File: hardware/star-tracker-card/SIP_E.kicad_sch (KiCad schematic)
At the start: 1 part, among them U7 OSD3358-512M-BSM

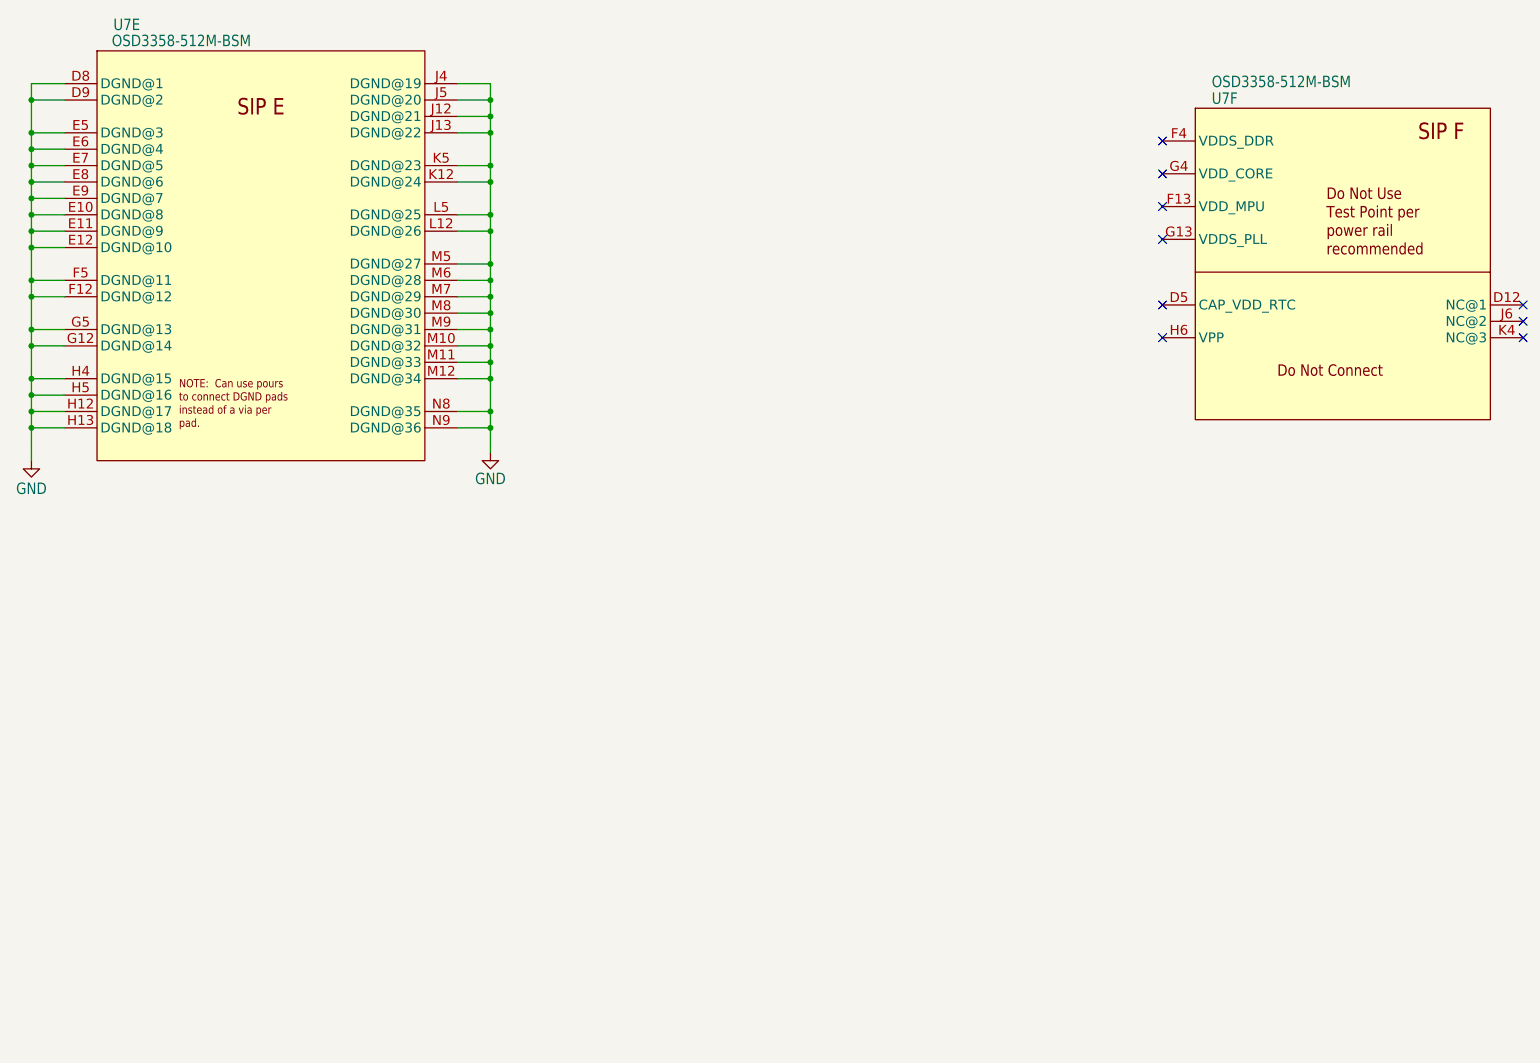
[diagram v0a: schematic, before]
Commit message: Big almost-done cleanup
Fixed a bunch of things in the schematic. Compared against C3 Octavo. Fixed all weird ERCs. Cleaned up a lot of planes on the layout. Moved uart switch, rerouted a bunch of traces for better layout. Fixed library issues, and board/sch sync issues.
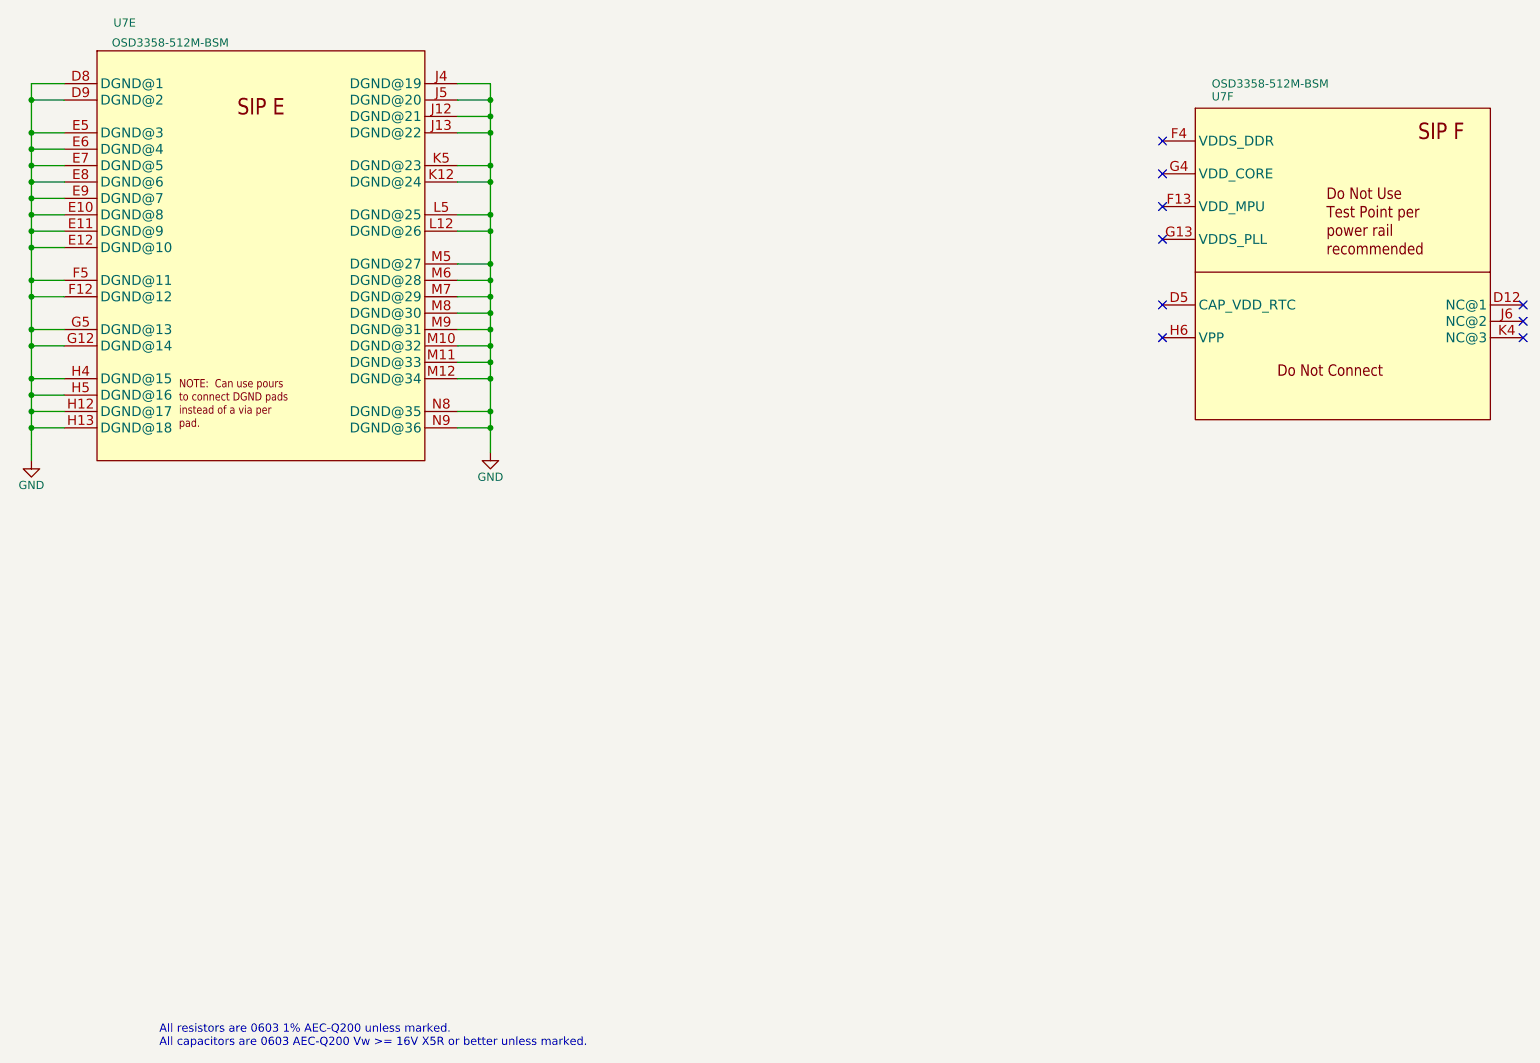
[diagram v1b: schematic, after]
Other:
- note added: "All resistors are 0603 1% AEC-Q200 unless marked. All capacitors are 0603 AEC-Q200 Vw >= 16V X5R or better unless marked."
- company: (none) -> Portland State Aerospace Society
- title: (none) -> OreSat Star Tracker
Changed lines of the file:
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@@
 	(generator_version "9.0")
 	(paper "B")
+	(title_block
+		(title "OreSat Star Tracker")
+		(date "2026-04-15")
+		(rev "1.3")
+		(company "Portland State Aerospace Society")
+	)
+	(text "All resistors are 0603 1% AEC-Q200 unless marked.\nAll capacitors are 0603 AEC-Q200 Vw >= 16V X5R or better unless marked."
+		(exclude_from_sim no)
+		(at 112.522 266.192 0)
+		(effects
+			(font
+				(size 1.27 1.27)
+			)
+			(justify left bottom)
+		)
+	)
 	(junction
 		(at 163.83 129.54)
@@
 			(effects
 				(font
-					(size 1.778 1.5113)
+					(size 1.27 1.27)
 				)
 				(justify left top)
@@
 			(effects
 				(font
-					(size 1.778 1.5113)
+					(size 1.27 1.27)
 				)
 				(justify left bottom)
@@
 		(on_board yes)
 		(dnp no)
-		(property "Reference" "#GND74"
-			(at 163.83 173.99 0)
+		(property "Reference" "#PWR74"
+			(at 163.83 180.34 0)
 			(effects
 				(font
@@
 		)
 		(property "Value" "GND"
-			(at 163.83 177.038 0)
+			(at 163.83 177.8 0)
 			(effects
 				(font
-					(size 1.778 1.5113)
-				)
-				(justify top)
+					(size 1.27 1.27)
+				)
 			)
 		)
@@
 			(project "star-tracker-card"
 				(path "/324e9eb5-7420-4b7e-862c-cc20bb28618a/eb575624-9a53-42ad-b889-70334a877908"
-					(reference "#GND74")
+					(reference "#PWR74")
 					(unit 1)
 				)
@@
 			(effects
 				(font
-					(size 1.778 1.5113)
+					(size 1.27 1.27)
 				)
 				(justify left top)
@@
 			(effects
 				(font
-					(size 1.778 1.5113)
+					(size 1.27 1.27)
 				)
 				(justify left bottom)
@@
 		(on_board yes)
 		(dnp no)
-		(property "Reference" "#GND73"
-			(at 92.71 175.26 0)
+		(property "Reference" "#PWR73"
+			(at 92.71 181.61 0)
 			(effects
 				(font
@@
 		)
 		(property "Value" "GND"
-			(at 92.71 178.562 0)
+			(at 92.71 179.07 0)
 			(effects
 				(font
-					(size 1.778 1.5113)
-				)
-				(justify top)
+					(size 1.27 1.27)
+				)
 			)
 		)
@@
 			(project "star-tracker-card"
 				(path "/324e9eb5-7420-4b7e-862c-cc20bb28618a/eb575624-9a53-42ad-b889-70334a877908"
-					(reference "#GND73")
+					(reference "#PWR73")
 					(unit 1)
 				)

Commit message: BOM 99% completed, push for final review
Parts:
- U7: DIS (none) -> DigiKey; DPN (none) -> 1676-OSD3358-1G-ISM-ND; MFR (none) -> Octavo Systems LLC; MPN (none) -> OSD3358-1G-ISM
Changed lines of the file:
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@@
 (kicad_sch
-	(version 20250114)
+	(version 20260306)
 	(generator "eeschema")
-	(generator_version "9.0")
+	(generator_version "10.0")
 	(paper "B")
 	(title_block
@@
 		(at 128.27 142.24 0)
 		(unit 5)
+		(body_style 1)
 		(exclude_from_sim no)
 		(in_bom yes)
 		(on_board yes)
+		(in_pos_files yes)
 		(dnp no)
 		(property "Reference" "U7"
 			(at 105.41 106.68 0)
+			(show_name no)
+			(do_not_autoplace no)
 			(effects
 				(font
@@
 		(property "Value" "OSD3358-512M-BSM"
 			(at 105.156 111.252 0)
+			(show_name no)
+			(do_not_autoplace no)
 			(effects
 				(font
@@
 		(property "Footprint" "star-tracker-card:OSD335X-BGA-256"
 			(at 128.27 142.24 0)
-			(effects
-				(font
-					(size 1.27 1.27)
-				)
-				(hide yes)
-			)
-		)
-		(property "Datasheet" ""
+			(hide yes)
+			(show_name no)
+			(do_not_autoplace no)
+			(effects
+				(font
+					(size 1.27 1.27)
+				)
+			)
+		)
+		(property "Datasheet" "https://octavosystems.com/docs/osd335x-sm-datasheet/"
 			(at 128.27 142.24 0)
-			(effects
-				(font
-					(size 1.27 1.27)
-				)
-				(hide yes)
-			)
-		)
-		(property "Description" "Octavo Systems LLC OSD335x Family SiP:  21mm x 21mm, 1.27mm pitch 256 pin BGA contains AM3358, 512MB DDR3, TPS65217, TL5209, 4KB EEPROM and passives.  Commerical Temperature (case):  0C to 85C."
+			(hide yes)
+			(show_name no)
+			(do_not_autoplace no)
+			(effects
+				(font
+					(size 1.27 1.27)
+				)
+			)
+		)
+		(property "Description" "OSD335x Embedded Module ARM® Cortex®-A8, AM3358 1GHz 1GB"
 			(at 128.27 142.24 0)
-			(effects
-				(font
-					(size 1.27 1.27)
-				)
-				(hide yes)
+			(hide yes)
+			(show_name no)
+			(do_not_autoplace no)
+			(effects
+				(font
+					(size 1.27 1.27)
+				)
+			)
+		)
+		(property "DIS" "DigiKey"
+			(at 128.27 142.24 0)
+			(hide yes)
+			(show_name no)
+			(do_not_autoplace no)
+			(effects
+				(font
+					(size 1.27 1.27)
+				)
+			)
+		)
+		(property "DPN" "1676-OSD3358-1G-ISM-ND"
+			(at 128.27 142.24 0)
+			(hide yes)
+			(show_name no)
+			(do_not_autoplace no)
+			(effects
+				(font
+					(size 1.27 1.27)
+				)
+			)
+		)
+		(property "MFR" "Octavo Systems LLC"
+			(at 128.27 142.24 0)
+			(hide yes)
+			(show_name no)
+			(do_not_autoplace no)
+			(effects
+				(font
+					(size 1.27 1.27)
+				)
+			)
+		)
+		(property "MPN" "OSD3358-1G-ISM"
+			(at 128.27 142.24 0)
+			(hide yes)
+			(show_name no)
+			(do_not_autoplace no)
+			(effects
+				(font
+					(size 1.27 1.27)
+				)
 			)
 		)
@@
 		(at 163.83 173.99 0)
 		(unit 1)
+		(body_style 1)
 		(exclude_from_sim no)
 		(in_bom yes)
 		(on_board yes)
+		(in_pos_files yes)
 		(dnp no)
 		(property "Reference" "#PWR74"
 			(at 163.83 180.34 0)
-			(effects
-				(font
-					(size 1.27 1.27)
-				)
-				(hide yes)
+			(hide yes)
+			(show_name no)
+			(do_not_autoplace no)
+			(effects
+				(font
+					(size 1.27 1.27)
+				)
 			)
 		)
 		(property "Value" "GND"
 			(at 163.83 177.8 0)
+			(show_name no)
+			(do_not_autoplace no)
 			(effects
 				(font
@@
 		(property "Footprint" ""
 			(at 163.83 173.99 0)
-			(effects
-				(font
-					(size 1.27 1.27)
-				)
-				(hide yes)
+			(hide yes)
+			(show_name no)
+			(do_not_autoplace no)
+			(effects
+				(font
+					(size 1.27 1.27)
+				)
 			)
 		)
 		(property "Datasheet" ""
 			(at 163.83 173.99 0)
-			(effects
-				(font
-					(size 1.27 1.27)
-				)
-				(hide yes)
+			(hide yes)
+			(show_name no)
+			(do_not_autoplace no)
+			(effects
+				(font
+					(size 1.27 1.27)
+				)
 			)
 		)
 		(property "Description" "Power symbol creates a global label with name \"GND\" , ground"
 			(at 163.83 173.99 0)
-			(effects
-				(font
-					(size 1.27 1.27)
-				)
-				(hide yes)
+			(hide yes)
+			(show_name no)
+			(do_not_autoplace no)
+			(effects
+				(font
+					(size 1.27 1.27)
+				)
 			)
 		)
@@
 		(at 295.91 146.05 0)
 		(unit 6)
+		(body_style 1)
 		(exclude_from_sim no)
 		(in_bom yes)
 		(on_board yes)
+		(in_pos_files yes)
 		(dnp no)
 		(property "Reference" "U7"
 			(at 275.59 118.11 0)
+			(show_name no)
+			(do_not_autoplace no)
 			(effects
 				(font
@@
 		(property "Value" "OSD3358-512M-BSM"
 			(at 275.59 117.602 0)
+			(show_name no)
+			(do_not_autoplace no)
 			(effects
 				(font
@@
 		(property "Footprint" "star-tracker-card:OSD335X-BGA-256"
 			(at 295.91 146.05 0)
-			(effects
-				(font
-					(size 1.27 1.27)
-				)
-				(hide yes)
-			)
-		)
-		(property "Datasheet" ""
+			(hide yes)
+			(show_name no)
+			(do_not_autoplace no)
+			(effects
+				(font
+					(size 1.27 1.27)
+				)
+			)
+		)
+		(property "Datasheet" "https://octavosystems.com/docs/osd335x-sm-datasheet/"
 			(at 295.91 146.05 0)
-			(effects
-				(font
-					(size 1.27 1.27)
-				)
-				(hide yes)
-			)
-		)
-		(property "Description" "Octavo Systems LLC OSD335x Family SiP:  21mm x 21mm, 1.27mm pitch 256 pin BGA contains AM3358, 512MB DDR3, TPS65217, TL5209, 4KB EEPROM and passives.  Commerical Temperature (case):  0C to 85C."
+			(hide yes)
+			(show_name no)
+			(do_not_autoplace no)
+			(effects
+				(font
+					(size 1.27 1.27)
+				)
+			)
+		)
+		(property "Description" "OSD335x Embedded Module ARM® Cortex®-A8, AM3358 1GHz 1GB"
 			(at 295.91 146.05 0)
-			(effects
-				(font
-					(size 1.27 1.27)
-				)
-				(hide yes)
+			(hide yes)
+			(show_name no)
+			(do_not_autoplace no)
+			(effects
+				(font
+					(size 1.27 1.27)
+				)
+			)
+		)
+		(property "DIS" "DigiKey"
+			(at 295.91 146.05 0)
+			(hide yes)
+			(show_name no)
+			(do_not_autoplace no)
+			(effects
+				(font
+					(size 1.27 1.27)
+				)
+			)
+		)
+		(property "DPN" "1676-OSD3358-1G-ISM-ND"
+			(at 295.91 146.05 0)
+			(hide yes)
+			(show_name no)
+			(do_not_autoplace no)
+			(effects
+				(font
+					(size 1.27 1.27)
+				)
+			)
+		)
+		(property "MFR" "Octavo Systems LLC"
+			(at 295.91 146.05 0)
+			(hide yes)
+			(show_name no)
+			(do_not_autoplace no)
+			(effects
+				(font
+					(size 1.27 1.27)
+				)
+			)
+		)
+		(property "MPN" "OSD3358-1G-ISM"
+			(at 295.91 146.05 0)
+			(hide yes)
+			(show_name no)
+			(do_not_autoplace no)
+			(effects
+				(font
+					(size 1.27 1.27)
+				)
 			)
 		)
@@
 		(at 92.71 175.26 0)
 		(unit 1)
+		(body_style 1)
 		(exclude_from_sim no)
 		(in_bom yes)
 		(on_board yes)
+		(in_pos_files yes)
 		(dnp no)
 		(property "Reference" "#PWR73"
 			(at 92.71 181.61 0)
-			(effects
-				(font
-					(size 1.27 1.27)
-				)
-				(hide yes)
+			(hide yes)
+			(show_name no)
+			(do_not_autoplace no)
+			(effects
+				(font
+					(size 1.27 1.27)
+				)
 			)
 		)
 		(property "Value" "GND"
 			(at 92.71 179.07 0)
+			(show_name no)
+			(do_not_autoplace no)
 			(effects
 				(font
@@
 		(property "Footprint" ""
 			(at 92.71 175.26 0)
-			(effects
-				(font
-					(size 1.27 1.27)
-				)
-				(hide yes)
+			(hide yes)
+			(show_name no)
+			(do_not_autoplace no)
+			(effects
+				(font
+					(size 1.27 1.27)
+				)
 			)
 		)
 		(property "Datasheet" ""
 			(at 92.71 175.26 0)
-			(effects
-				(font
-					(size 1.27 1.27)
-				)
-				(hide yes)
+			(hide yes)
+			(show_name no)
+			(do_not_autoplace no)
+			(effects
+				(font
+					(size 1.27 1.27)
+				)
 			)
 		)
 		(property "Description" "Power symbol creates a global label with name \"GND\" , ground"
 			(at 92.71 175.26 0)
-			(effects
-				(font
-					(size 1.27 1.27)
-				)
-				(hide yes)
-			)
-		)
+			(hide yes)
+			(show_name no)
+			(do_not_autoplace no)
+			(effects
+				(font
+					(size 1.27 1.27)
+				)
+			)
+		)
